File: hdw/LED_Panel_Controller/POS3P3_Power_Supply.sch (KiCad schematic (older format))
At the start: 27 parts

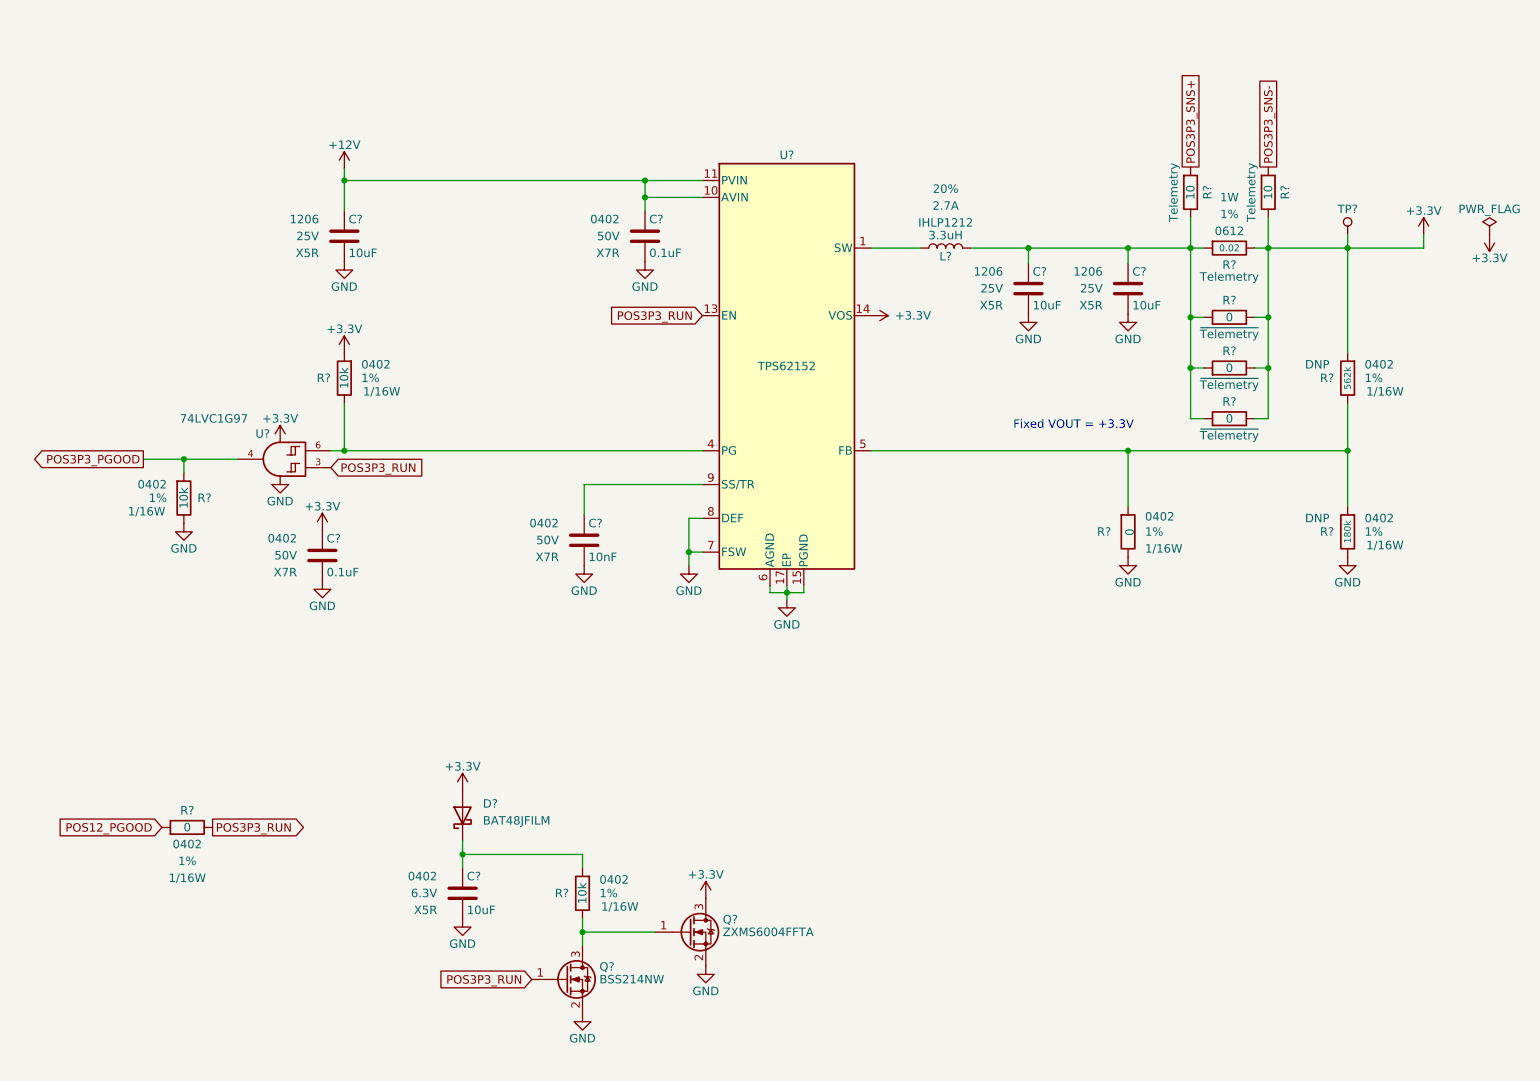
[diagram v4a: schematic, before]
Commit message: assigned I2C addresses
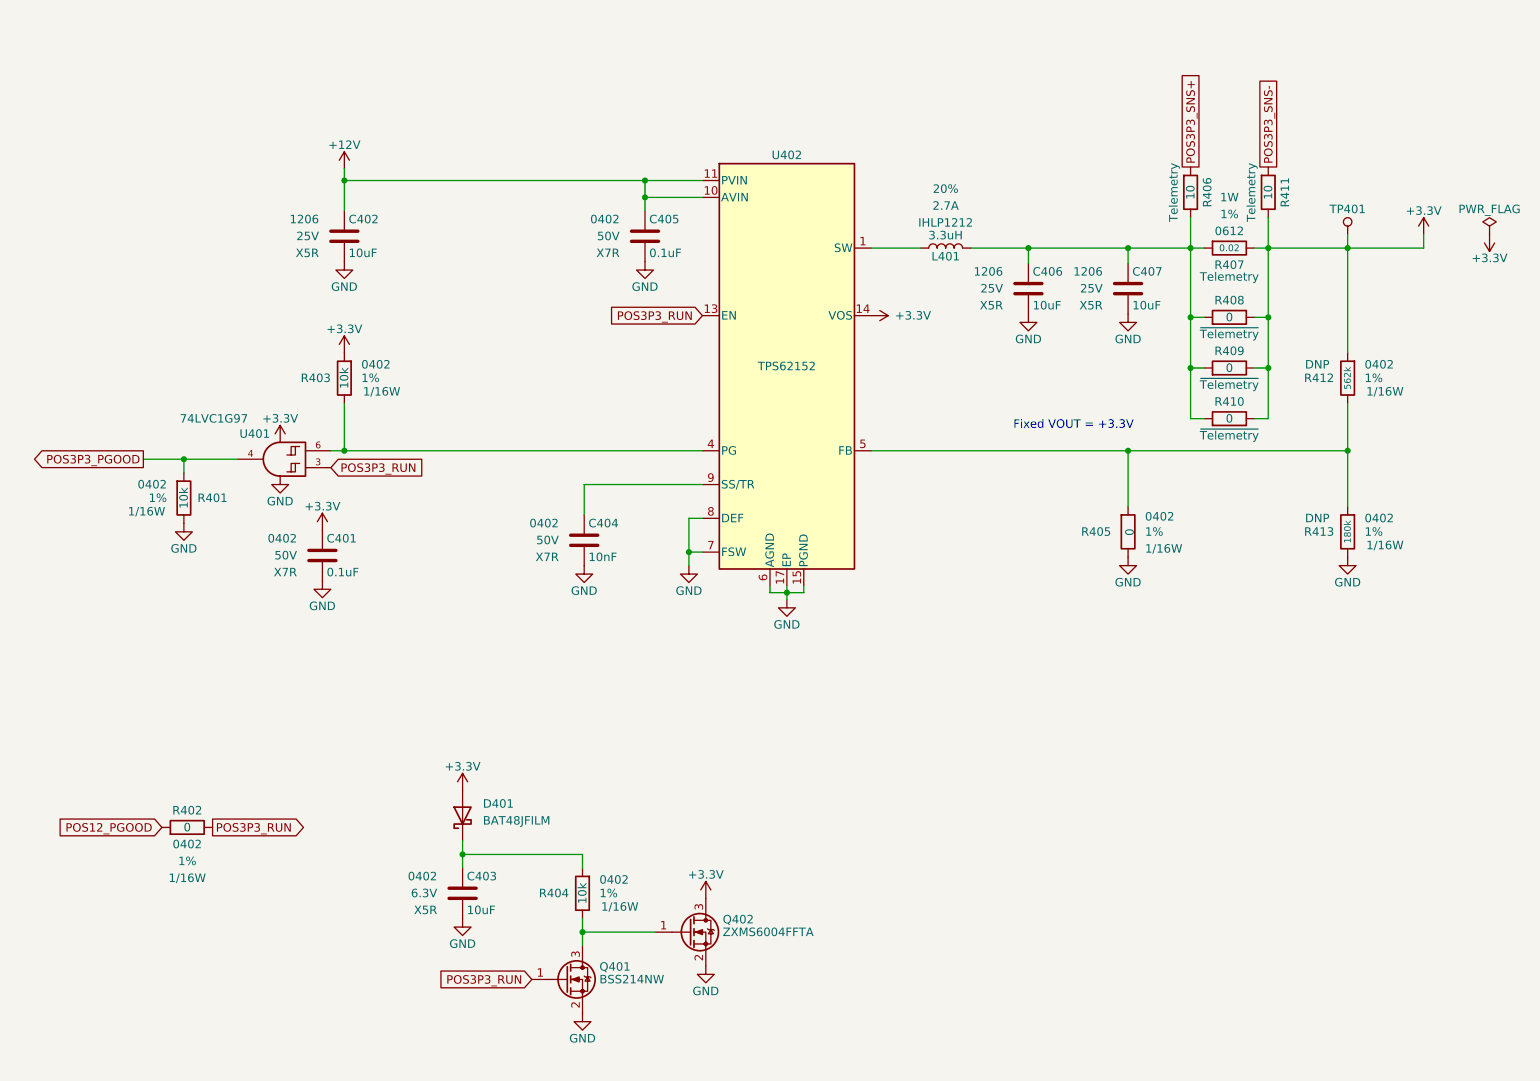
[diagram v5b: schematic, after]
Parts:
- removed C?: 0.1uF, Capacitors_SMD:C_0402, symbol Custom_Library:C_Custom
- removed C?: 10uF, Capacitors_SMD:C_1206, symbol Custom_Library:C_Custom
- removed R?: 0.02, Resistors_SMD:R_0612, symbol Custom_Library:R_Custom
- removed R?: 10k, Resistors_SMD:R_0402, symbol Custom_Library:R_Custom
- removed R?: 180k, Resistors_SMD:R_0402, symbol Custom_Library:R_Custom
- removed R?: 10, Resistors_SMD:R_0402, symbol Custom_Library:R_Custom
- removed R? (x4): 0, Resistors_SMD:R_0402, symbol Custom_Library:R_Custom
- removed TP?: TP, Custom Footprints Library:Test_Point, symbol Custom_Library:TP
- removed U?: 74LVC1G97, Package_TO_SOT_SMD:SOT-363_SC-70-6, symbol Custom_Library:74LVC1G97_Power_AND
- added C405: 0.1uF, Capacitors_SMD:C_0402, symbol Custom_Library:C_Custom
- added C407: 10uF, Capacitors_SMD:C_1206, symbol Custom_Library:C_Custom
- added R403: 10k, Resistors_SMD:R_0402, symbol Custom_Library:R_Custom
- added R405, R408, R409, R410: 0, Resistors_SMD:R_0402, symbol Custom_Library:R_Custom
- added R406: 10, Resistors_SMD:R_0402, symbol Custom_Library:R_Custom
- added R407: 0.02, Resistors_SMD:R_0612, symbol Custom_Library:R_Custom
- added R413: 180k, Resistors_SMD:R_0402, symbol Custom_Library:R_Custom
- added TP401: TP, Custom Footprints Library:Test_Point, symbol Custom_Library:TP
- added U401: 74LVC1G97, Package_TO_SOT_SMD:SOT-363_SC-70-6, symbol Custom_Library:74LVC1G97_Power_AND
- gave numbers to parts that had none: 15
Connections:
- net +12V: now also C405.1
- net +3V3: now also R403.1, R407.2, R408.2, R409.2, R410.2, TP401.1 (TP), U401.5 (VCC)
- net GND: now also C405.2, C407.2, R405.2, R413.2, U401.1 (GND), U401.2 (GND)
- net POS3P3_PGOOD: now also U401.4
- net POS3P3_RUN: now also U401.3
- net POS3P3_SNS+: now also R406.1
- net at C406.1, L401.2: now also C407.1, R406.2, R407.1, R408.1, R409.1, R410.1
- net at R412.2, U402.5 (FB): now also R405.1, R413.1
- net at U402.4 (PG): now also R403.2, U401.6

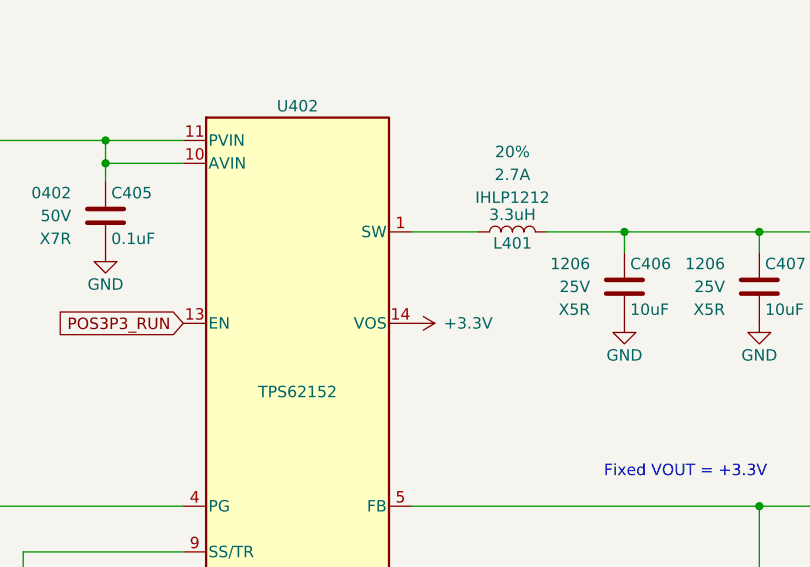
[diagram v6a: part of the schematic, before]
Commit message: USB/power PCB grouping
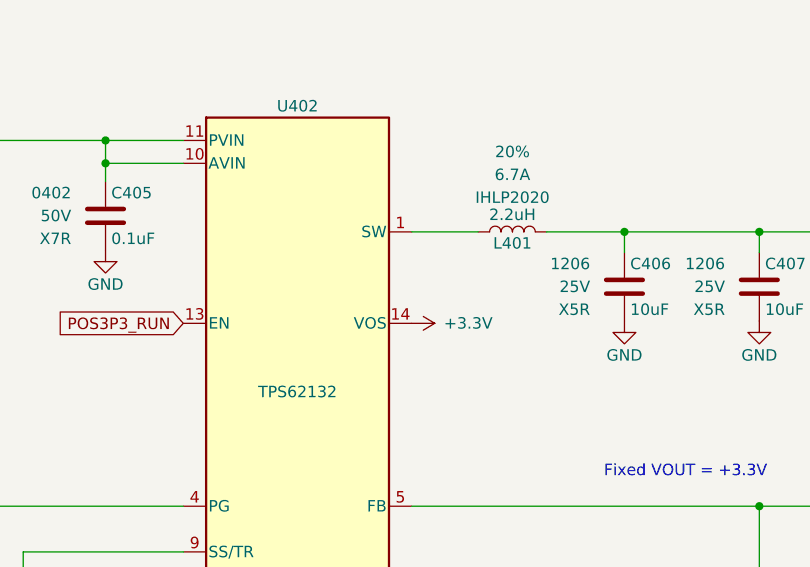
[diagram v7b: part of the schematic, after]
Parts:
- removed U402: TPS62152, Package_DFN_QFN:QFN-16-1EP_3x3mm_P0.5mm_EP1.8x1.8mm, symbol Custom_Library:TPS62150
- added U402: TPS62132, Package_DFN_QFN:QFN-16-1EP_3x3mm_P0.5mm_EP1.8x1.8mm, symbol Custom_Library:TPS62130
- L401: value 3.3uH -> 2.2uH; footprint Inductors_SMD:L_Vishay_IHLP-1212 -> Inductors_SMD:L_Vishay_IHLP-2020; Ampacity 2.7A -> 6.7A; Digi-Key PN 541-2567-1-ND -> 541-1236-1-ND; display_footprint IHLP1212 -> IHLP2020
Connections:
- net +12V: now also U402.10 (AVIN), U402.11 (PVIN), U402.12 (PVIN)
- net +3V3: now also U402.14 (VOS)
- net GND: now also U402.15 (PGND), U402.16 (PGND), U402.17 (EP), U402.6 (AGND), U402.7 (FSW), U402.8 (DEF)
- net POS3P3_RUN: now also U402.13 (EN)
- net at L401.1: now also U402.1 (SW), U402.2 (SW), U402.3 (SW)
- net at R405.1, R412.2, R413.1: now also U402.5 (FB)
- net at C404.1: now also U402.9 (SS/TR)
- net at R403.2, U401.6: now also U402.4 (PG)
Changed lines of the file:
@@
 $EndDescr
-$Comp
-L Custom_Library:L_Custom L?
-U 1 1 5C26EF0D
-P 6330 3040
-AR Path="/5CB7718D/5C26EF0D" Ref="L?"  Part="1"
-AR Path="/5E0DC082/5C26EF0D" Ref="L?"  Part="1"
-AR Path="/5E0F263A/5C26EF0D" Ref="L?"  Part="1"
-AR Path="/5EAE2D8A/5C26EF0D" Ref="L?"  Part="1"
-AR Path="/5F581B64/5C26EF0D" Ref="L401"  Part="1"
-F 0 "L401" V 6280 3040 50  0000 C CNN
-F 1 "3.3uH" V 6405 3040 50  0000 C CNN
-F 2 "Inductors_SMD:L_Vishay_IHLP-1212" H 6330 3040 50  0001 C CNN
-F 3 "" H 6330 3040 50  0001 C CNN
-F 4 "541-2567-1-ND" H 6330 3040 50  0001 C CNN "Digi-Key PN"
-F 5 "IHLP1212" V 6480 3040 50  0000 C CNN "display_footprint"
-F 6 "2.7A" V 6580 3040 50  0000 C CNN "Ampacity"
-F 7 "20%" V 6680 3040 50  0000 C CNN "Tolerance"
-	1    6330 3040
-	0    -1   -1   0
-$EndComp
 $Comp
 L Custom_Library:C_Custom C?
@@
 Text GLabel 1690 6470 0    50   Input ~ 0
 POS12_PGOOD
-$Comp
-L Custom_Library:TPS62150 U402
-U 1 1 5EB8DB31
-P 5390 3740
-F 0 "U402" H 5390 4990 50  0000 C CNN
-F 1 "TPS62152" H 5390 3740 50  0000 C CNN
-F 2 "Package_DFN_QFN:QFN-16-1EP_3x3mm_P0.5mm_EP1.8x1.8mm" H 5390 3740 50  0001 C CNN
-F 3 "https://www.ti.com/lit/ds/symlink/tps62150.pdf?&ts=1589125931316" H 5390 3740 50  0001 C CNN
-F 4 "296-43621-1-ND" H 5390 3740 50  0001 C CNN "Digi-Key PN"
-	1    5390 3740
-	1    0    0    -1
-$EndComp
 Wire Wire Line
 	8710 3960 8710 4240
@@
 	1    0    0    -1
 $EndComp
+$Comp
+L Custom_Library:TPS62130 U?
+U 1 1 6076F50F
+P 5390 3740
+AR Path="/6076F50F" Ref="U?"  Part="1"
+AR Path="/5F581BA3/6076F50F" Ref="U?"  Part="1"
+AR Path="/5F581B64/6076F50F" Ref="U402"  Part="1"
+F 0 "U402" H 5390 4990 50  0000 C CNN
+F 1 "TPS62132" H 5390 3740 50  0000 C CNN
+F 2 "Package_DFN_QFN:QFN-16-1EP_3x3mm_P0.5mm_EP1.8x1.8mm" H 5390 3740 50  0001 C CNN
+F 3 "http://www.ti.com/lit/ds/symlink/tps62130.pdf" H 5390 3740 50  0001 C CNN
+F 4 "296-29936-1-ND" H 5390 3740 50  0001 C CNN "Digi-Key PN"
+	1    5390 3740
+	1    0    0    -1
+$EndComp
+$Comp
+L Custom_Library:L_Custom L?
+U 1 1 60771D26
+P 6330 3040
+AR Path="/60771D26" Ref="L?"  Part="1"
+AR Path="/5F581BA3/60771D26" Ref="L?"  Part="1"
+AR Path="/5F581B64/60771D26" Ref="L401"  Part="1"
+F 0 "L401" V 6280 3040 50  0000 C CNN
+F 1 "2.2uH" V 6405 3040 50  0000 C CNN
+F 2 "Inductors_SMD:L_Vishay_IHLP-2020" H 6330 3040 50  0001 C CNN
+F 3 "" H 6330 3040 50  0001 C CNN
+F 4 "IHLP2020" V 6480 3040 50  0000 C CNN "display_footprint"
+F 5 "6.7A" V 6580 3040 50  0000 C CNN "Ampacity"
+F 6 "20%" V 6680 3040 50  0000 C CNN "Tolerance"
+F 7 "541-1236-1-ND" H 6330 3040 50  0001 C CNN "Digi-Key PN"
+	1    6330 3040
+	0    -1   -1   0
+$EndComp
 $EndSCHEMATC
